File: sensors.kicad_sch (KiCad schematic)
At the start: 6 parts, among them U3 ICM-42688-P, U5 MCP98243

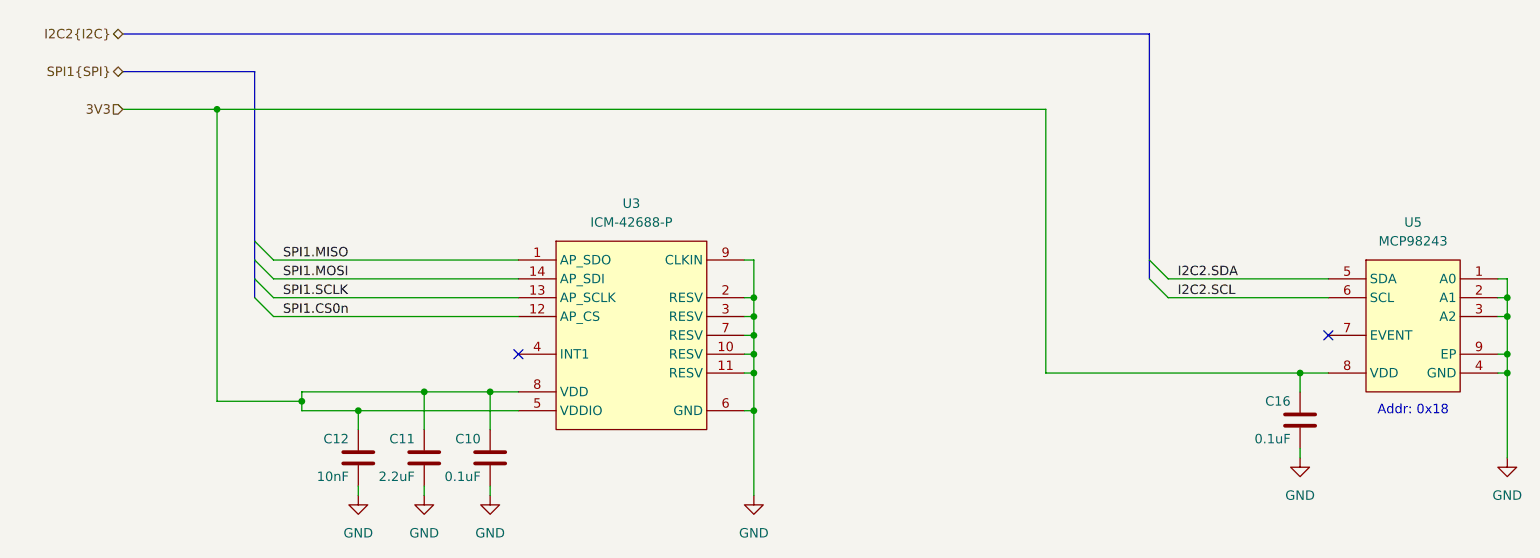
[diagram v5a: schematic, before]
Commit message: added fabrication outputs, replaced imu drop-in og imu was out of stock everywhere, invensense drop-in replacement
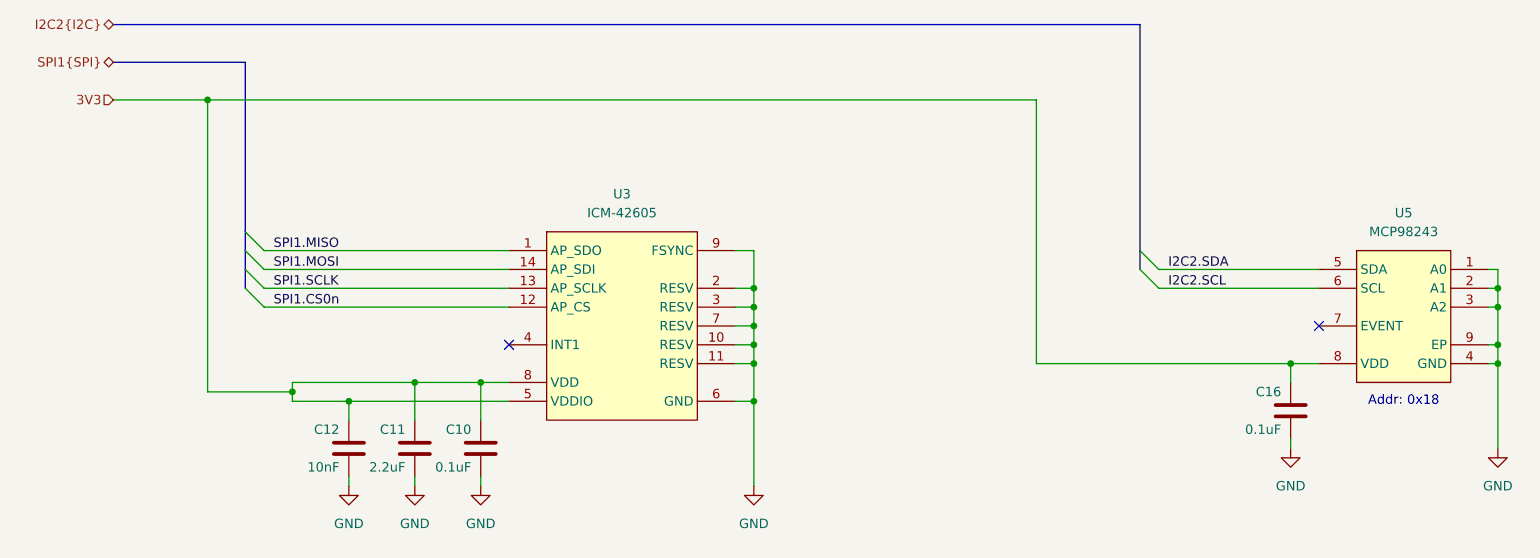
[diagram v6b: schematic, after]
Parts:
- removed U3: ICM-42688-P, Package_LGA:LGA-14_3x2.5mm_P0.5mm_LayoutBorder3x4y, symbol library:ICM-42688-P
- added U3: ICM-42605, Package_LGA:LGA-14_3x2.5mm_P0.5mm_LayoutBorder3x4y, symbol library:ICM-42605
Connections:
- net 3V3: now also U3.5 (VDDIO), U3.8 (VDD)
- net GND: now also U3.10 (RESV), U3.11 (RESV), U3.2 (RESV), U3.3 (RESV), U3.6 (GND), U3.7 (RESV), U3.9 (FSYNC)
- net SPI1.CS0n: now also U3.12 (AP_CS)
- net SPI1.MISO: now also U3.1 (AP_SDO)
- net SPI1.MOSI: now also U3.14 (AP_SDI)
- net SPI1.SCLK: now also U3.13 (AP_SCLK)
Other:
- moved on the sheet: C10, C11, C12, C16, U5
